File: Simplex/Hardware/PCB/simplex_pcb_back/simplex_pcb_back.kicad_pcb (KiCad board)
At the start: 2 copper layers, 20 x 100 mm, 16 parts, among them J1 Conn_02x06_Odd_Even, J5 Conn_01x07_Male, J6 Conn_01x03_Male, U1 TL072, U2 MCP6002-xP, U3 MCP4922

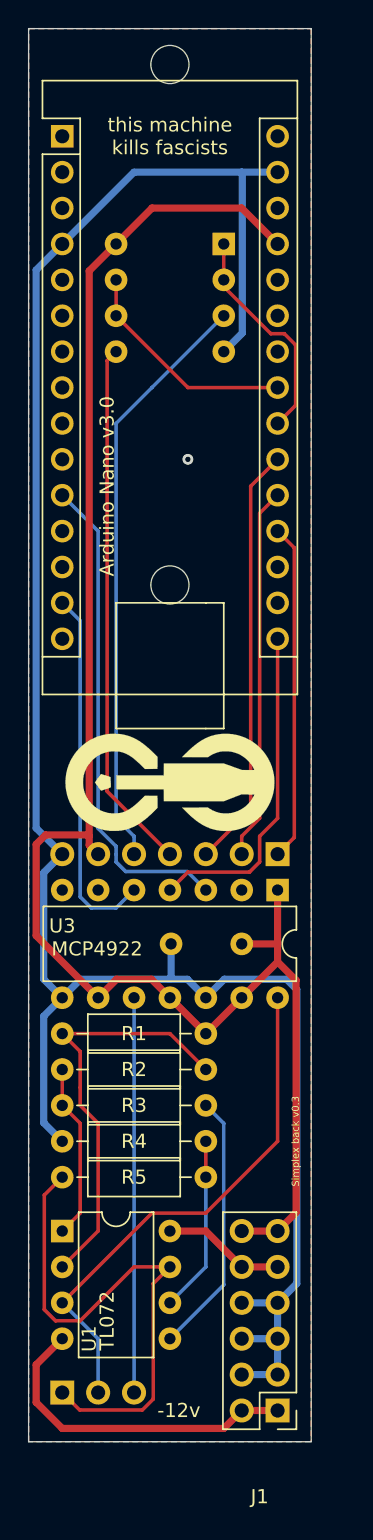
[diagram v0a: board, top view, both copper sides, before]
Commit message: updated and converted simplex to new kicad version
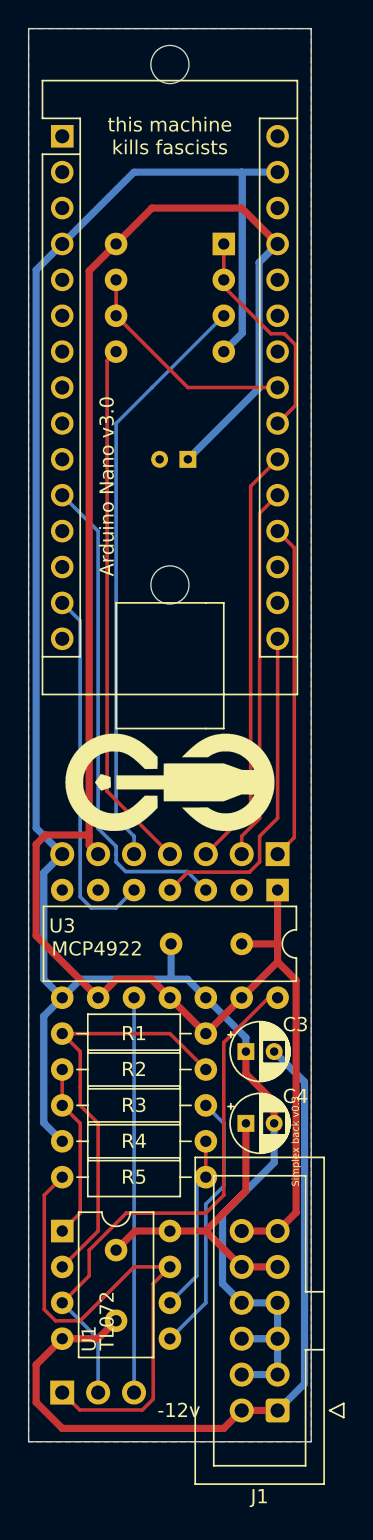
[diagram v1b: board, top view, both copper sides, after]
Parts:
- added C2: 100nF, Capacitor_THT:C_Disc_D4.3mm_W1.9mm_P5.00mm, B.Cu at (46.2, 126.4)
- added C3: 10uF, Capacitor_THT:CP_Radial_D4.0mm_P2.00mm, F.Cu at (55.4, 112.4)
- added C4: 10uF, Capacitor_THT:CP_Radial_D4.0mm_P2.00mm, F.Cu at (55.4, 117.5)
- added C5: 10uF, Capacitor_THT:CP_Radial_D4.0mm_P2.00mm, B.Cu at (51.3, 70.5)
- J1: footprint Connector_PinHeader_2.54mm:PinHeader_2x06_P2.54mm_Vertical -> Connector_IDC:IDC-Header_2x06_P2.54mm_Vertical
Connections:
- A1 pad 1: Net-(A1-Pad1) -> unconnected-(A1-D1/TX-Pad1)
- A1 pad 10: Net-(A1-Pad10) -> unconnected-(A1-D7-Pad10)
- A1 pad 12: Net-(A1-Pad12) -> unconnected-(A1-D9-Pad12)
- A1 pad 13: Net-(A1-Pad13) -> unconnected-(A1-D10-Pad13)
- A1 pad 15: Net-(A1-Pad15) -> unconnected-(A1-D12-Pad15)
- A1 pad 17: Net-(A1-Pad17) -> unconnected-(A1-3V3-Pad17)
- A1 pad 18: Net-(A1-Pad18) -> unconnected-(A1-AREF-Pad18)
- A1 pad 2: Net-(A1-Pad2) -> unconnected-(A1-D0/RX-Pad2)
- A1 pad 24: Net-(A1-Pad24) -> unconnected-(A1-A5-Pad24)
- A1 pad 25: Net-(A1-Pad25) -> unconnected-(A1-A6-Pad25)
- A1 pad 26: Net-(A1-Pad26) -> unconnected-(A1-A7-Pad26)
- A1 pad 28: Net-(A1-Pad28) -> unconnected-(A1-~{RESET}-Pad28)
- A1 pad 3: Net-(A1-Pad3) -> unconnected-(A1-~{RESET}-Pad3)
- A1 pad 30: Net-(A1-Pad30) -> unconnected-(A1-VIN-Pad30)
- A1 pad 5: Net-(A1-Pad5) -> unconnected-(A1-D2-Pad5)
- A1 pad 6: Net-(A1-Pad6) -> unconnected-(A1-D3-Pad6)
- A1 pad 7: Net-(A1-Pad7) -> unconnected-(A1-D4-Pad7)
- A1 pad 8: Net-(A1-Pad8) -> unconnected-(A1-D5-Pad8)
- A1 pad 9: Net-(A1-Pad9) -> unconnected-(A1-D6-Pad9)
- U3 pad 2: Net-(U3-Pad2) -> unconnected-(U3-NC-Pad2)
- U3 pad 6: Net-(U3-Pad6) -> unconnected-(U3-NC-Pad6)
- U3 pad 7: Net-(U3-Pad7) -> unconnected-(U3-NC-Pad7)
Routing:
- net -12V: track 23.6 -> 55.1 mm
- net +5V: track 121.7 -> 139.6 mm
- net +12V: track 8.67 -> 21.8 mm
- net GND: track 154.3 -> 150.0 mm, vias 1 -> 0
- net DAC_OUT_A: track 37.5 -> 39.0 mm
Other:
- net class Default removed
- net class Power removed
- board text added: "Simplex back v0.3.1"
